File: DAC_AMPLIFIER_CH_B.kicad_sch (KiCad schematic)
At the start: 26 parts, among them IC50 ${DEVICE}, IC51 ${DEVICE}, IC52 ${DEVICE}

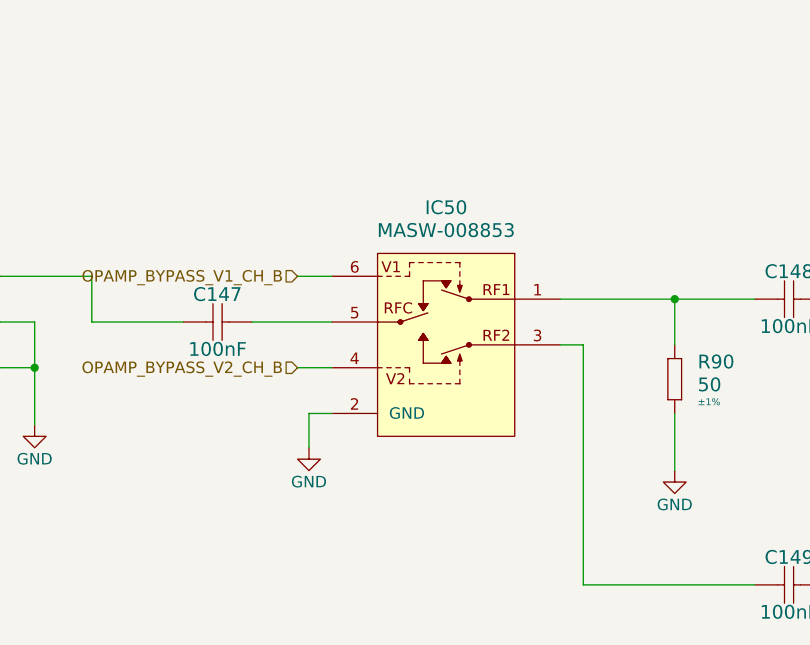
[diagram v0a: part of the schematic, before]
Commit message: Updated schematic and rerouted PCB
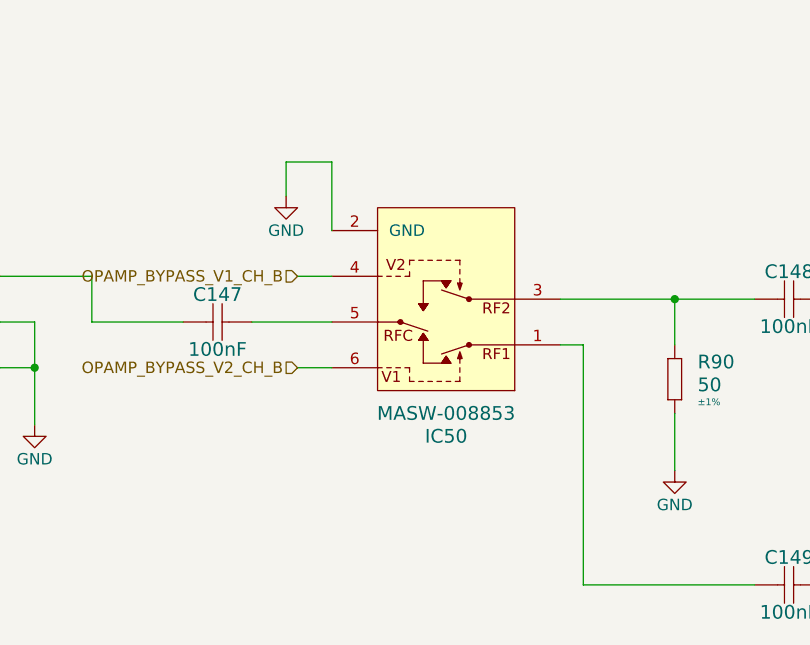
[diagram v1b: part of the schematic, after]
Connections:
- net OPAMP_BYPASS_V1_CH_B: now also IC50.4 (V2); no longer IC50.6 (V1)
- net OPAMP_BYPASS_V2_CH_B: now also IC50.6 (V1); no longer IC50.4 (V2)
- net at C148.1, R90.2: now also IC50.3 (RF2); no longer IC50.1 (RF1)
- net at C149.1: now also IC50.1 (RF1); no longer IC50.3 (RF2)
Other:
- moved on the sheet: IC50
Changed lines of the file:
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@@
 	(wire
 		(pts
-			(xy 114.3 116.84) (xy 114.3 120.65)
+			(xy 111.76 88.9) (xy 111.76 92.71)
 		)
 		(stroke
@@
 	(wire
 		(pts
-			(xy 116.84 116.84) (xy 114.3 116.84)
+			(xy 111.76 88.9) (xy 116.84 88.9)
 		)
 		(stroke
@@
 	(wire
 		(pts
+			(xy 116.84 88.9) (xy 116.84 96.52)
+		)
+		(stroke
+			(width 0)
+			(type default)
+		)
+	)
+	(wire
+		(pts
 			(xy 198.12 78.74) (xy 210.82 78.74)
 		)
@@
 	(symbol
 		(lib_id "CERN:Analog & Interface/MASW-008853")
-		(at 121.92 99.06 0)
+		(at 121.92 114.3 0)
+		(mirror x)
 		(unit 1)
 		(exclude_from_sim no)
@@
 		(on_board yes)
 		(dnp no)
-		(fields_autoplaced yes)
 		(property "Reference" "IC50"
-			(at 129.54 93.98 0)
+			(at 129.54 119.38 0)
 			(effects
 				(font
@@
 		)
 		(property "Value" "${DEVICE}"
-			(at 129.54 96.52 0)
+			(at 129.54 116.84 0)
 			(effects
 				(font
@@
 		)
 		(property "Footprint" "ICs And Semiconductors SMD:SOT65P210X110-6N"
-			(at 121.92 99.06 0)
+			(at 121.92 114.3 0)
 			(effects
 				(font
@@
 		)
 		(property "Datasheet" "${CERN_DATASHEET_DIR}\\MASW-008853.pdf"
-			(at 121.92 99.06 0)
+			(at 121.92 114.3 0)
 			(effects
 				(font
@@
 		)
 		(property "Description" "GaAs SPDT 2.7 V High Power Switch DC - 5.0 GHz"
-			(at 121.92 99.06 0)
+			(at 121.92 114.3 0)
 			(effects
 				(font
@@
 		)
 		(property "Manufacturer" "MACOM"
-			(at 121.92 99.06 0)
+			(at 121.92 114.3 0)
 			(show_name yes)
 			(effects
@@
 		)
 		(property "Comment" "MASW-008853"
-			(at 121.92 99.06 0)
+			(at 121.92 114.3 0)
 			(show_name yes)
 			(effects
@@
 		)
 		(property "Component Kind" "Standard"
-			(at 121.92 99.06 0)
+			(at 121.92 114.3 0)
 			(show_name yes)
 			(effects
@@
 		)
 		(property "Component Type" "Standard"
-			(at 121.92 99.06 0)
+			(at 121.92 114.3 0)
 			(show_name yes)
 			(effects
@@
 		)
 		(property "Device" "MASW-008853"
-			(at 121.92 99.06 0)
+			(at 121.92 114.3 0)
 			(show_name yes)
 			(effects
@@
 		)
 		(property "PackageDescription" "SOT363, SC70-6, 0.65mm Pitch; 6 pin, 1.25mm W X 2.00mm L X 1.10mm H body, IPC Medium Density"
-			(at 121.92 99.06 0)
+			(at 121.92 114.3 0)
 			(show_name yes)
 			(effects
@@
 		)
 		(property "Status" ""
-			(at 121.92 99.06 0)
+			(at 121.92 114.3 0)
 			(show_name yes)
 			(effects
@@
 		)
 		(property "Part Description" "GaAs SPDT 2.7 V High Power Switch DC - 5.0 GHz"
-			(at 121.92 99.06 0)
+			(at 121.92 114.3 0)
 			(show_name yes)
 			(effects
@@
 		)
 		(property "Manufacturer Part Number" "MASW-008853"
-			(at 121.92 99.06 0)
+			(at 121.92 114.3 0)
 			(show_name yes)
 			(effects
@@
 		)
 		(property "Pin Count" "6"
-			(at 121.92 99.06 0)
+			(at 121.92 114.3 0)
 			(show_name yes)
 			(effects
@@
 		)
 		(property "Case" "SOT363"
-			(at 121.92 99.06 0)
+			(at 121.92 114.3 0)
 			(show_name yes)
 			(effects
@@
 		)
 		(property "Mounted" "Yes"
-			(at 121.92 99.06 0)
+			(at 121.92 114.3 0)
 			(show_name yes)
 			(effects
@@
 		)
 		(property "Socket" "No"
-			(at 121.92 99.06 0)
+			(at 121.92 114.3 0)
 			(show_name yes)
 			(effects
@@
 		)
 		(property "SMD" "Yes"
-			(at 121.92 99.06 0)
+			(at 121.92 114.3 0)
 			(show_name yes)
 			(effects
@@
 		)
 		(property "PressFit" "No"
-			(at 121.92 99.06 0)
+			(at 121.92 114.3 0)
 			(show_name yes)
 			(effects
@@
 		)
 		(property "Sense" "No"
-			(at 121.92 99.06 0)
+			(at 121.92 114.3 0)
 			(show_name yes)
 			(effects
@@
 		)
 		(property "Sense Comment" ""
-			(at 121.92 99.06 0)
+			(at 121.92 114.3 0)
 			(show_name yes)
 			(effects
@@
 		)
 		(property "Bonding" "No"
-			(at 121.92 99.06 0)
+			(at 121.92 114.3 0)
 			(show_name yes)
 			(effects
@@
 		)
 		(property "Status Comment" ""
-			(at 121.92 99.06 0)
+			(at 121.92 114.3 0)
 			(show_name yes)
 			(effects
@@
 		)
 		(property "ComponentHeight" "1.1mm"
-			(at 121.92 99.06 0)
+			(at 121.92 114.3 0)
 			(show_name yes)
 			(effects
@@
 		)
 		(property "Author" "CERN DEM HF"
-			(at 121.92 99.06 0)
+			(at 121.92 114.3 0)
 			(show_name yes)
 			(effects
@@
 		)
 		(property "HelpURL" "\\\\cern.ch\\dfs\\Applications\\Altium\\Datasheets\\MASW-008853.pdf"
-			(at 121.92 99.06 0)
+			(at 121.92 114.3 0)
 			(show_name yes)
 			(effects
@@
 		)
 		(property "ComponentLink1URL" ""
-			(at 121.92 99.06 0)
+			(at 121.92 114.3 0)
 			(show_name yes)
 			(effects
@@
 		)
 		(property "ComponentLink2URL" ""
-			(at 121.92 99.06 0)
+			(at 121.92 114.3 0)
 			(show_name yes)
 			(effects
@@
 		)
 		(property "ComponentLink2Description" ""
-			(at 121.92 99.06 0)
+			(at 121.92 114.3 0)
 			(show_name yes)
 			(effects
@@
 		)
 		(property "ComponentLink1Description" ""
-			(at 121.92 99.06 0)
+			(at 121.92 114.3 0)
 			(show_name yes)
 			(effects
@@
 		)
 		(property "CreateDate" "2025-07-10 00:00:00 +0000"
-			(at 121.92 99.06 0)
+			(at 121.92 114.3 0)
 			(show_name yes)
 			(effects
@@
 		)
 		(property "LatestRevisionDate" "2025-07-10 00:00:00 +0000"
-			(at 121.92 99.06 0)
+			(at 121.92 114.3 0)
 			(show_name yes)
 			(effects
@@
 		)
 		(property "SCEM" ""
-			(at 121.92 99.06 0)
+			(at 121.92 114.3 0)
 			(show_name yes)
 			(effects
@@
 		)
 		(property "LatestRevisionDate1" ""
-			(at 121.92 99.06 0)
+			(at 121.92 114.3 0)
 			(show_name yes)
 			(effects
@@
 		)
 		(property "Field1" ""
-			(at 121.92 99.06 0)
+			(at 121.92 114.3 0)
 			(show_name yes)
 			(effects
@@
 		)
 		(property "LibSymbol" "Analog & Interface:MASW-008853"
-			(at 121.92 99.06 0)
+			(at 121.92 114.3 0)
 			(show_name yes)
 			(effects
@@
 		)
 		(property "LibFootprint" "ICs And Semiconductors SMD:SOT65P210X110-6N"
-			(at 121.92 99.06 0)
+			(at 121.92 114.3 0)
 			(show_name yes)
 			(effects
@@
 		)
 		(property "Part Number" "MASW-008853"
-			(at 121.92 99.06 0)
+			(at 121.92 114.3 0)
 			(effects
 				(font
@@
 		)
 		(property "Database Name" "ICs And Semiconductors_Backup"
-			(at 121.92 99.06 0)
+			(at 121.92 114.3 0)
 			(effects
 				(font
@@
 		)
 		(property "Database Table Name" "Analog & Interface"
-			(at 121.92 99.06 0)
+			(at 121.92 114.3 0)
 			(effects
 				(font
@@
 		)
 		(property "Part Number Nocolon" "MASW-008853"
-			(at 121.92 99.06 0)
+			(at 121.92 114.3 0)
 			(effects
 				(font
@@
 	(symbol
 		(lib_id "power:GND")
-		(at 114.3 120.65 0)
+		(at 111.76 92.71 0)
 		(mirror y)
 		(unit 1)
@@
 		(dnp no)
 		(property "Reference" "#PWR0243"
-			(at 114.3 127 0)
+			(at 111.76 99.06 0)
 			(effects
 				(font
@@
 		)
 		(property "Value" "GND"
-			(at 114.3 124.46 0)
+			(at 111.76 96.52 0)
 			(effects
 				(font
@@
 		)
 		(property "Footprint" ""
-			(at 114.3 120.65 0)
+			(at 111.76 92.71 0)
 			(effects
 				(font
@@
 		)
 		(property "Datasheet" ""
-			(at 114.3 120.65 0)
+			(at 111.76 92.71 0)
 			(effects
 				(font
@@
 		)
 		(property "Description" "Power symbol creates a global label with name \"GND\" , ground"
-			(at 114.3 120.65 0)
+			(at 111.76 92.71 0)
 			(effects
 				(font

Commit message: Rerouted PCB Logic part
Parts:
- renumbered C145 to C1501, C146 to C1502, C147 to C1503, C148 to C1504, C149 to C1505, C150 to C1506, C151 to C1507, C152 to C1508, C153 to C1509, C154 to C1510, C155 to C1511, C156 to C1512, C157 to C1513, C158 to C1514, IC50 to IC1501, IC51 to IC1502, IC52 to IC1503, L25 to L1501, R90 to R1501, R91 to R1502, R92 to R1503, R93 to R1504, R94 to R1505, R95 to R1506, R96 to R1507, TR8 to TR1501
